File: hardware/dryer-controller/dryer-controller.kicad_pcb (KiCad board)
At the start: 2 copper layers, 110 x 85 mm, 69 parts, among them K1 SRD-05VDC-SL-C, K2 SRD-05VDC-SL-C, Q1 MMBT2222A, Q2 MMBT2222A, Q3 CJ2310, Q4 CJ2310, Q5 CJ2310, SW1 SW-USB, U1 K7805-1000R3

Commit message: Make the fab-order files match what is fitted
U1's value was K7805-1000R3 while the fitted part is the TRACO TSR 1-2450
from Mouser; the value is now TSR 1-2450 and the description names the
Mouser source and the MornSun part as the unstocked alternative. The
hardware.md BOM row follows.

Test points TP1-TP9 were in the BOM with no LCSC number, contradicting
"test points are not parts"; the schematic now marks them not in BOM, so
the BOM designators equal the CPL's exactly and every BOM line but U1
carries an LCSC number (both tests red on the old schematic).

The release step attached out/*.csv, which picks up KiCad's own position
file; it now attaches the -bom and -cpl files only, and releasing.md
drops the position-CSV wording. kicad/kicad:10.0.6 exists on Docker Hub,
so CI pins it: the TP2 placement works round a DRC false positive seen
in 10.0.6.

Co-Authored-By: Claude Opus 5.5 <noreply@anthropic.com>
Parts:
- U1: value K7805-1000R3 -> TSR 1-2450
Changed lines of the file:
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@@
 			)
 		)
-		(property "Value" "K7805-1000R3"
+		(property "Value" "TSR 1-2450"
 			(at 2.5 3.25 0)
 			(layer "F.Fab")

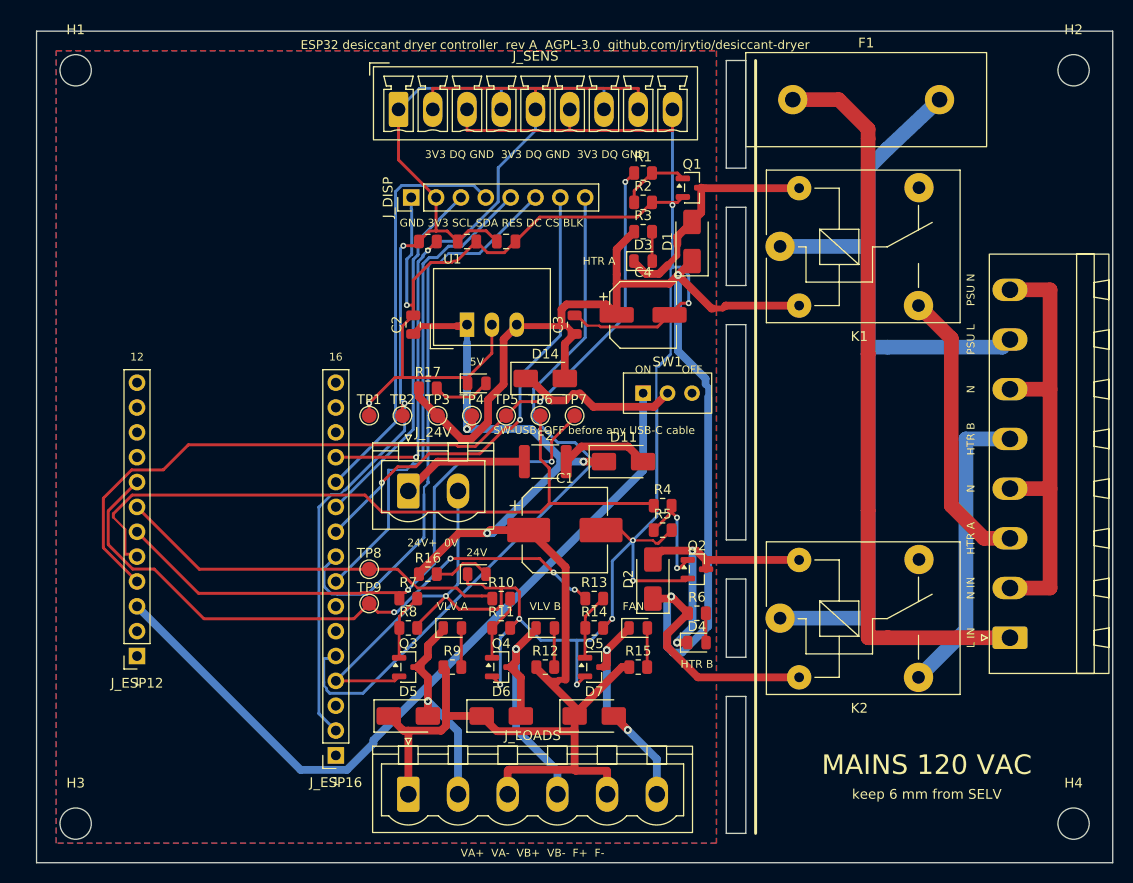
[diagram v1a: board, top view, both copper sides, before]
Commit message: Split the design into a controller board and a mains board (review of 2026-10-15)
The single 110 x 85 mm board becomes two: dryer-controller (76 x 85 mm:
the socketed Thing Plus, 24 V in, the 5 V module, SW-USB, the three MOSFET
stages, sensor and display headers, test points) and dryer-mains (64 x 85
mm: F1, both relays with their driver stages, J_MAINS), joined by the
protoboard harness's keyed JST-XH 4-way link (J_RLY / J_CTRL: 5 V, GND,
heater A, heater B). The 1 k base series resistors stay on the controller
and the pulldowns on the mains board, as the protoboard had them. The mains
board is the single board's mains strip moved 48 mm left and 6 mm down on a
2 mm wider board, so the measured clearances hold.

Review items: F1 is a 22.5 mm-pitch footprint with slotted holes (21.5 to
23.5 mm) for the BLX-A style holders on hand, hand-fitted; the PTF-76-B
15 mm footprint stays in the library. U1 is the Amazon-sourced TSR 1-2450,
hand-fitted, with a bench check of its pin order added to the first-article
check. Mounting holes are 4.3 mm (M4) on both boards. The SHT45 stays on
the Thing Plus's Qwiic connector (firmware and pins verified, documented).
PCBWay feasibility is written up in hardware/README.md (advice only).

Generator: circuit.py and placement.py become parts.py (catalogue and
helpers), controller.py and mains.py (each board's parts, nets, geometry,
silk; mains rules and copper in mains.py) and boards.py; every command runs
over both boards unless one is named. The local footprints move to
hardware/lib/dryer.pretty and are copied into each project; the sync check
compares the copies. Outputs and review renders are per board. The board
tests hold one generator-built board at a time: building a second
invalidates the first in pcbnew.

Docs: hardware.md PCB section, board-continuity-check.md PCB section, the
spec's as-built addendum, hardware/README.md, CLAUDE.md, README, releasing,
failure modes, inspection checklist, datasheets (PTF-77, BLX-A, JST XH).

Co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
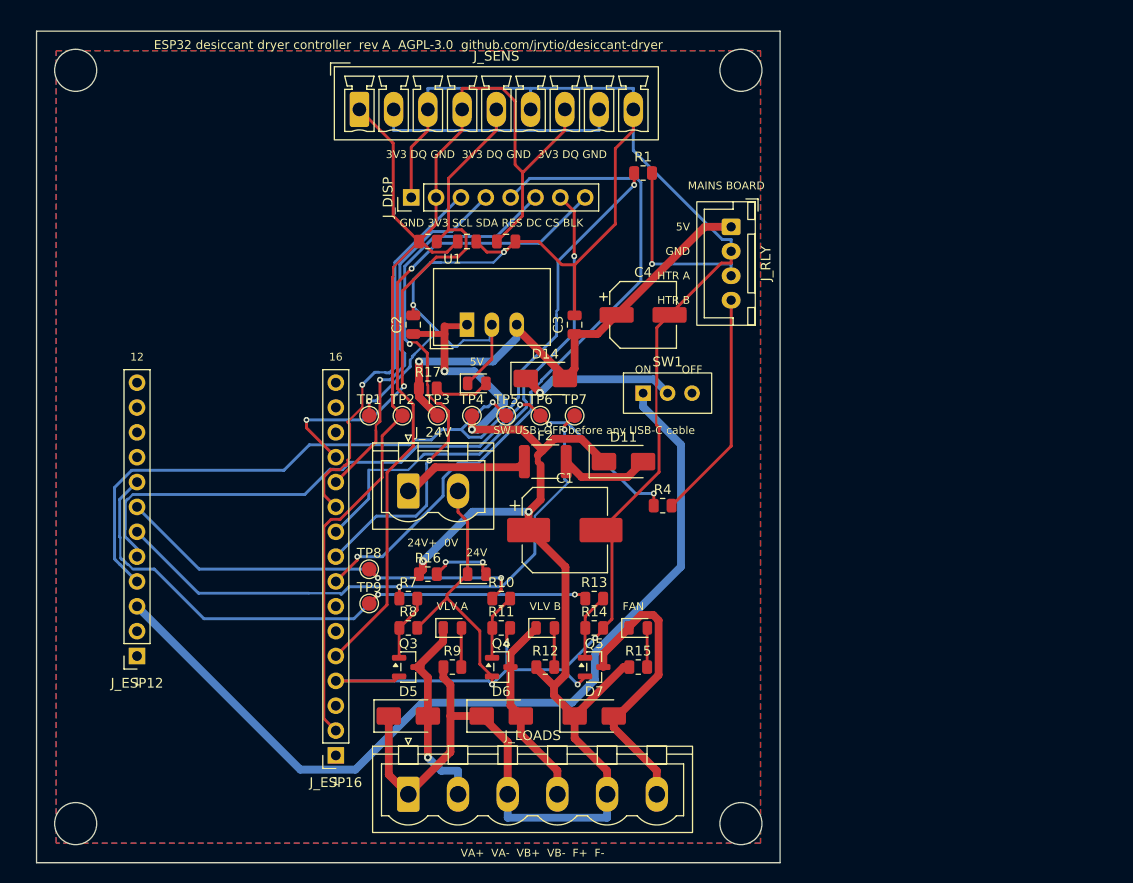
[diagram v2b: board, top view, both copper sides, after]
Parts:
- removed D1, D2: S1M, Diode_SMD:D_SMA
- removed D3, D4: LED red, LED_SMD:LED_0805_2012Metric
- removed F1: T 3.15 A 5x20, dryer:Fuseholder_5x20mm_Covered_XFCN_PTF-76-B_P15.00mm
- removed J_MAINS: 120 VAC, dryer:PhoenixContact_MSTBA_2,5_8-G-5,08_1x08_P5.08mm_Horizontal_Drill1.7mm
- removed K1, K2: SRD-05VDC-SL-C, Relay_THT:Relay_SPDT_SANYOU_SRD_Series_Form_C
- removed Q1, Q2: MMBT2222A, Package_TO_SOT_SMD:SOT-23
- removed R2, R5: 1k, Resistor_SMD:R_0805_2012Metric
- removed R3, R6: 2.2k, Resistor_SMD:R_0805_2012Metric
- added J_RLY: to mains board, Connector_JST:JST_XH_B4B-XH-A_1x04_P2.50mm_Vertical, F.Cu at (71.0, 20.0)
- H1, H2, H3, H4: value M3 -> M4; footprint MountingHole:MountingHole_3.2mm_M3 -> MountingHole:MountingHole_4.3mm_M4
- moved H2 34.0 mm to (72.0, 4.00)
- moved H4 34.0 mm to (72.0, 81.0)
- moved J_SENS 4.00 mm to (33.0, 8.00)
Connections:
- R1 pad 2: BASE_A -> RLY_A
- R4 pad 2: BASE_B -> RLY_B
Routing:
- net +5V: track 144.2 -> 51.7 mm, vias 2 -> 1
- net L_FUSED: track 88.9 -> 0.00 mm
- net L_IN: track 75.4 -> 0.00 mm
- net N: track 46.9 -> 0.00 mm
- net L_SW_B: track 30.9 -> 0.00 mm
- net L_SW_A: track 29.2 -> 0.00 mm
- net COIL_B: track 27.8 -> 0.00 mm, vias 2 -> 0
- net COIL_A: track 23.8 -> 0.00 mm
- net RLY_B: track 0.00 -> 23.5 mm
- net GND: track 275.6 -> 253.7 mm, vias 11 -> 7
- net LCD_RST: track 49.4 -> 70.8 mm, vias 0 -> 1
- net RLY_A: track 0.00 -> 18.6 mm, vias 0 -> 1
- net +3V3: track 107.8 -> 124.2 mm, vias 2 -> 0
- net VBUS: track 79.4 -> 92.1 mm
- net BASE_B: track 10.6 -> 0.00 mm, vias 2 -> 0
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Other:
- board size 110 x 85 mm -> 76 x 85 mm
- board text added: "MAINS BOARD"
- board text removed: "L IN"
- board text removed: "MAINS 120 VAC"
- board text removed: "N"
- board text removed: "N IN"
- board text removed: "PSU L"
- board text removed: "PSU N"
- board text removed: "keep 6 mm from SELV"

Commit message: Fit the controller and mains boards to 85 x 70 and 45 x 70 mm
The reviewer's enclosure spaces are 85 x 70 mm (controller) and 45 x 70 mm
(mains); the split boards were 76 x 85 and 64 x 85. New tests pin the
outlines before DRC: each board's declared size and Edge.Cuts geometry,
the corner holes 4 mm in, every courtyard inside the outline (the ESP
sockets, J_MAINS and the M4 head courtyards excepted), no hole under the
Thing Plus body, and the same link pinout on J_RLY and J_CTRL.

Controller: the Thing Plus lies along the long edge, USB-C face 3 mm past
the left edge, antenna keep-out at the right end starting past the last
socket pads (a no-pads keep-out cannot cover them). J_RLY and J_SENS on
the right edge clear of the M4 courtyards; J_24V, J_DISP (along the edge)
and J_LOADS at the bottom; the 5 V block, 24 V chain and MOSFET stages in
between. Silk re-pointed; the title moves to the back, and the edge
connectors' references are hidden behind their pin legends.

Mains: SELV strip x 0-7 in two columns, slot x 7-9 with gaps at the coil
pads, relays with COM at x 12, F1 across the top at y 14 (the J_MAINS
courtyard and H2's fix it there), J_MAINS pads at x 39.5 with N linked on
the plug side. MAINS_TRACKS re-laid with the rev A arrangement and
distances (measured): 6.27 mm to SELV outside the relay areas, 3.5 inside,
1.8 mm L to L, 1.1 mm L to N, 7.8 mm from F1 to H2's hole edge. The GND
pour starts at y 21 so its outline, not a rules-aware refill, keeps F1
6.7 mm from it: board.build fills before the project's rules exist. The
relay-area spine tests in test_project follow the new spine and areas.

Both boards regenerated fresh and unrouted; DRC shows only unconnected
items. test_routed_board's DRC-clean and fully-routed checks fail until
the boards are routed (next task).

Co-Authored-By: Claude Opus 5.5 <noreply@anthropic.com>
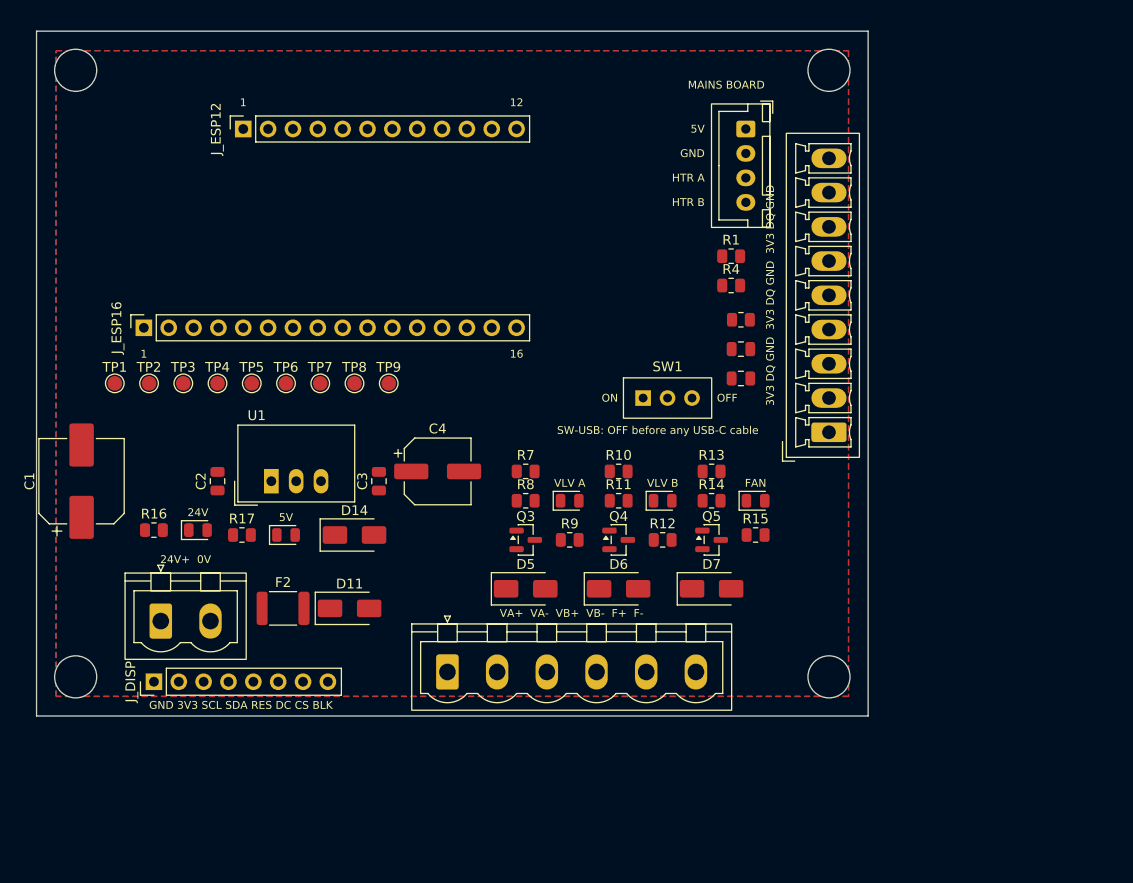
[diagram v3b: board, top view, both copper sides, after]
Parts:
- moved J_SENS 58.2 mm to (81.0, 41.0), turned to 90 degrees
- moved J_DISP 56.1 mm to (12.0, 66.5)
- moved J_ESP12 55.0 mm to (21.1, 10.0), turned to 90 degrees
- moved C1 49.7 mm to (4.60, 46.0), turned to 90 degrees
- moved J_ESP16 47.9 mm to (11.0, 30.3), turned to 90 degrees
- moved R18 33.0 mm to (72.0, 29.5)
- moved D11 31.8 mm to (32.0, 59.0)
- moved F2 30.7 mm to (25.2, 59.0)
- moved C5 30.1 mm to (72.0, 32.5)
- moved D12 28.9 mm to (16.5, 51.0)
- moved J_24V 28.6 mm to (12.7, 60.3)
- moved R16 28.4 mm to (12.0, 51.0)
- moved C6 27.8 mm to (72.0, 35.5)
- moved C4 26.4 mm to (41.0, 45.0)
- moved TP1 26.2 mm to (8.00, 36.0)
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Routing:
- net GND: track 253.7 -> 0.00 mm, vias 7 -> 0
- net +24V: track 155.7 -> 0.00 mm, vias 4 -> 0
- net +3V3: track 124.2 -> 0.00 mm
- net VBUS: track 92.1 -> 0.00 mm
- net HTR_A: track 90.6 -> 0.00 mm, vias 2 -> 0
- net OW_DQ: track 81.5 -> 0.00 mm, vias 2 -> 0
- net LCD_RST: track 70.8 -> 0.00 mm, vias 1 -> 0
- net HTR_B: track 69.7 -> 0.00 mm, vias 3 -> 0
- net LCD_BL: track 64.9 -> 0.00 mm, vias 1 -> 0
- net VLV_A: track 62.4 -> 0.00 mm, vias 2 -> 0
- net FAN: track 61.1 -> 0.00 mm, vias 2 -> 0
- net LCD_DC: track 55.9 -> 0.00 mm, vias 2 -> 0
- net +5V: track 51.7 -> 0.00 mm, vias 1 -> 0
- net LCD_CS: track 50.8 -> 0.00 mm, vias 1 -> 0
- net VLV_B: track 44.0 -> 0.00 mm, vias 2 -> 0
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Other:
- board size 76 x 85 mm -> 85 x 70 mm

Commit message: Route both boards at their enclosure sizes
Both boards are routed with Freerouting 2.5.0 (200 passes) and are DRC
clean with every pad connected: controller 477 tracks, mains 171.

The router copy now carries what the router could not see:
- a 0.55 mm keep-out band inside the outline, since Freerouting keeps
  only its 0.2 mm clearance from the edge and the project needs 0.5;
- a keep-out round each mains pad or track outside the relay areas,
  grown by 5.85 mm (6.05 with the router's own clearance), so SELV
  routes in the strip keep the 6 mm "mains to selv" rule beside F1's
  pad 1 (6.07 mm measured, COIL_A).
After the import, a track the optimiser necked below the project's
0.2 mm minimum (two 0.18 mm LCD_RST pieces, with room for 0.3) goes
back to its netclass width; DRC judges the result.

The saved pour fill now honours the project rules: board.build and
route.route refill and save through kicad-cli (drc --refill-zones
--save-board) once the .kicad_pro and .kicad_dru are on disk, then
put the canonical .kicad_pro back. Before, the pcbnew filler ran with
only the zone's own 0.3 mm clearance, so DRC's refill could pass while
the copper the gerbers are plotted from sat closer to mains. The gerber
and SVG exports pass --check-zones. Two tests: the committed mains
board's GND fill keeps 6 mm from mains copper outside the relay areas
and 3.5 inside, and a scratch mains board with the pour drawn 3.9 mm
from F1's pad 1 comes out of board.build pulled back (it fails with
the refill disabled).

Co-Authored-By: Claude Opus 5.5 <noreply@anthropic.com>
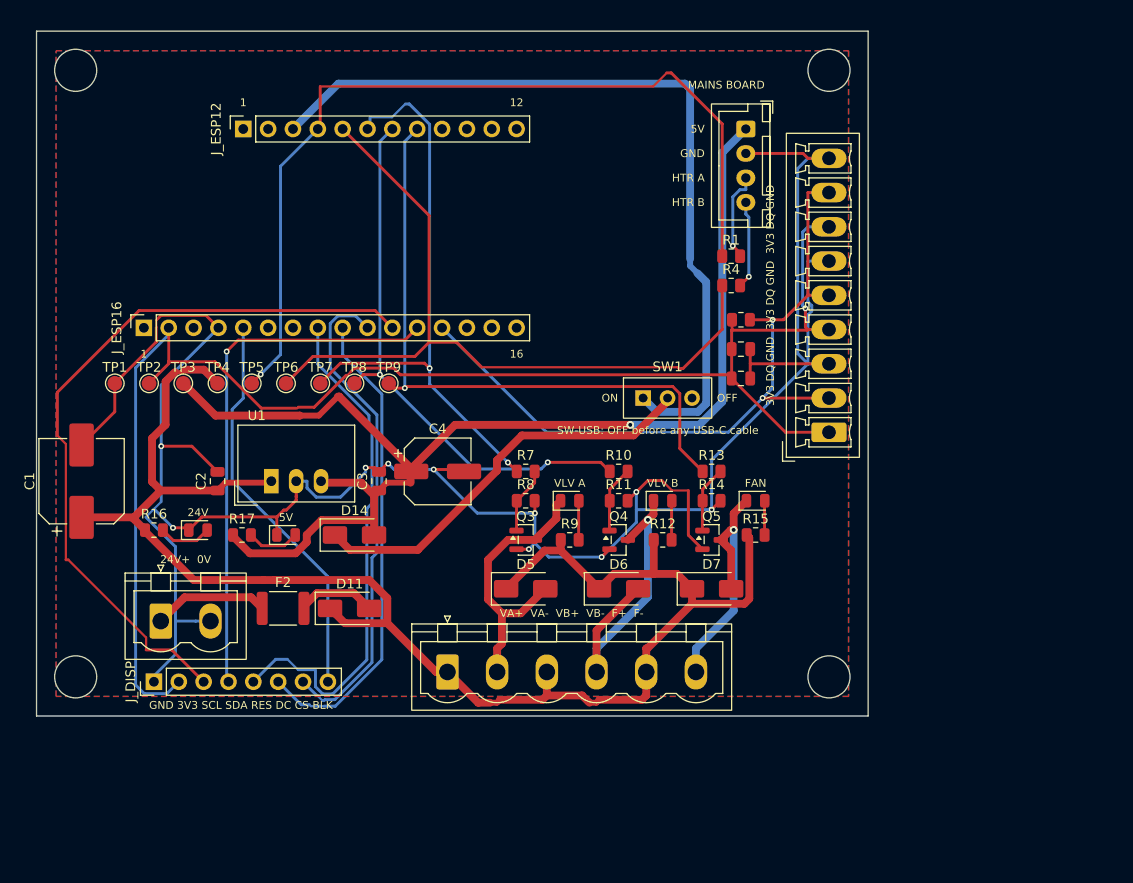
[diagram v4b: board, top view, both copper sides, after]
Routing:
- net GND: track 0.00 -> 252.2 mm, vias 0 -> 10
- net +24V: track 0.00 -> 164.9 mm
- net +3V3: track 0.00 -> 152.5 mm, vias 0 -> 1
- net +5V: track 0.00 -> 125.0 mm, vias 0 -> 1
- net HTR_A: track 0.00 -> 90.6 mm, vias 0 -> 1
- net VBUS: track 0.00 -> 83.0 mm
- net HTR_B: track 0.00 -> 79.0 mm
- net SPI_CLK: track 0.00 -> 75.9 mm
- net OW_DQ: track 0.00 -> 75.6 mm, vias 0 -> 2
- net FAN: track 0.00 -> 66.2 mm, vias 0 -> 1
- net VLV_A: track 0.00 -> 60.2 mm, vias 0 -> 2
- net VLV_B: track 0.00 -> 56.7 mm, vias 0 -> 2
- net SPI_MOSI: track 0.00 -> 54.3 mm, vias 0 -> 1
- net LCD_RST: track 0.00 -> 52.9 mm
- net LCD_CS: track 0.00 -> 50.9 mm
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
